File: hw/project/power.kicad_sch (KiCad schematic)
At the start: 28 parts, among them Q1 MOSFET, N-CH, SINGLE, 120A, 6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, Q2 MOSFET, N-CH, SINGLE, 120A, 6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, U1 TLV74033PDBVR, U3 LM74502DDFR, U4 LMR51610XDBVR

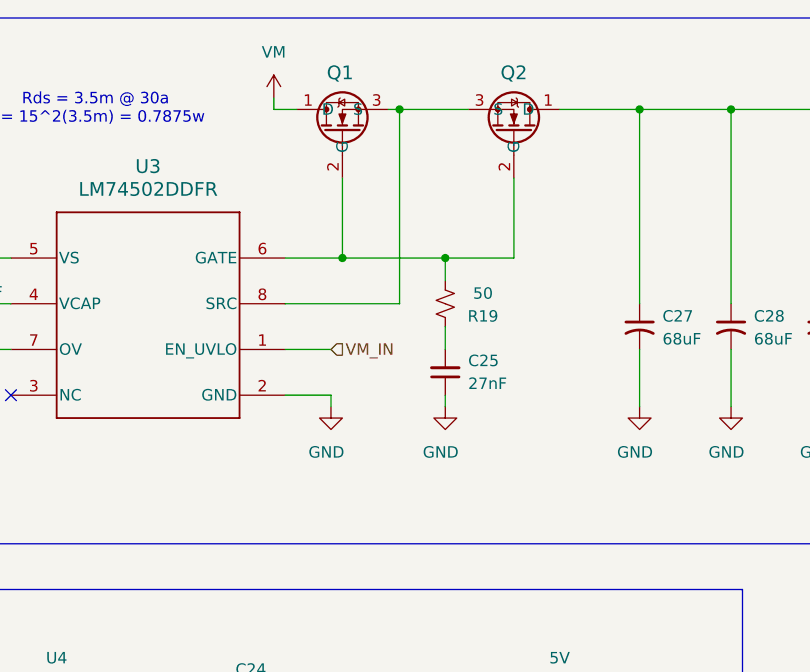
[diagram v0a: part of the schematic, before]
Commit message: Wire PWR BTN
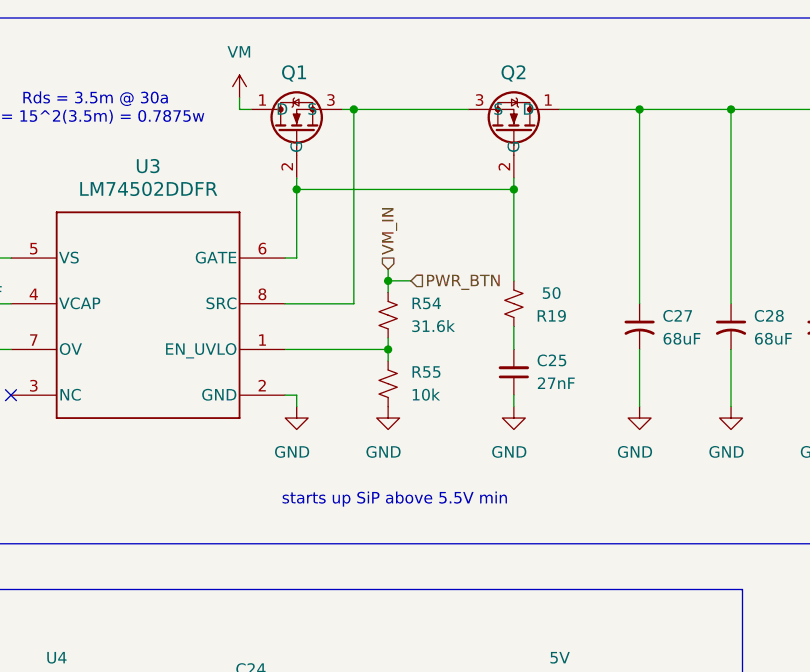
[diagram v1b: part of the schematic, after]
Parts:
- added R54: 31.6k, symbol Device:R_Small_US
- added R55: 10k, symbol Device:R_Small_US
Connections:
- net GND: now also R55.2
- net VM_IN renamed PWR_BTN
- net PWR_BTN: now also R54.1; no longer U3.1 (EN_UVLO)
- new net: R54.2, R55.1, U3.1 (EN_UVLO)
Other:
- note added: "starts up SiP above 5.5V min"
- moved on the sheet: C25, Q1, R19

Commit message: Add comment to 5V buck
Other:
- note added: "Rds = 3.5m @ 30a P = 30^2(3.5m) = 3.15w"
- note added: "are you sure this gives 5V? can you document the calculation for getting 5V output?"
- note removed: "Rds = 3.5m @ 30a P = 15^2(3.5m) = 0.7875w"
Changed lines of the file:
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@@
 		)
 	)
-	(text "Rds = 3.5m @ 30a\nP = 15^2(3.5m) = 0.7875w"
+	(text "Rds = 3.5m @ 30a\nP = 30^2(3.5m) = 3.15w"
 		(exclude_from_sim no)
 		(at 89.408 33.02 0)
@@
 			)
 		)
+	)
+	(text "are you sure this gives 5V?\n\ncan you document the calculation\nfor getting 5V output?"
+		(exclude_from_sim no)
+		(at 127 129.032 0)
+		(effects
+			(font
+				(size 1.27 1.27)
+				(color 255 4 4 1)
+			)
+		)

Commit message: Leo's final revisions to (mostly) periphs
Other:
- note added: "<- add (hookable, if appropriate) test points where you can in the Power sheet"
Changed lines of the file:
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@@
+		)
+	)
+	(text "<- add (hookable, if appropriate) test points \nwhere you can in the Power sheet"
+		(exclude_from_sim no)
+		(at 241.808 108.458 0)
+		(effects
+			(font
+				(size 1.27 1.27)
+				(color 255 4 4 1)
+			)
 		)
 	)

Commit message: Update sheet settings
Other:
- company: (none) -> Electrium Mobility
- title: (none) -> ESC 2026 - Power
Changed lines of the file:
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@@
 	(paper "A4")
 	(title_block
+		(title "ESC 2026 - Power")
 		(date "2026-02-20")
-		(rev "1")
+		(rev "v3")
+		(company "Electrium Mobility")
 		(comment 1 "Author: Nelson Mei, Arnav Shah, Eleanor Wang")
 	)

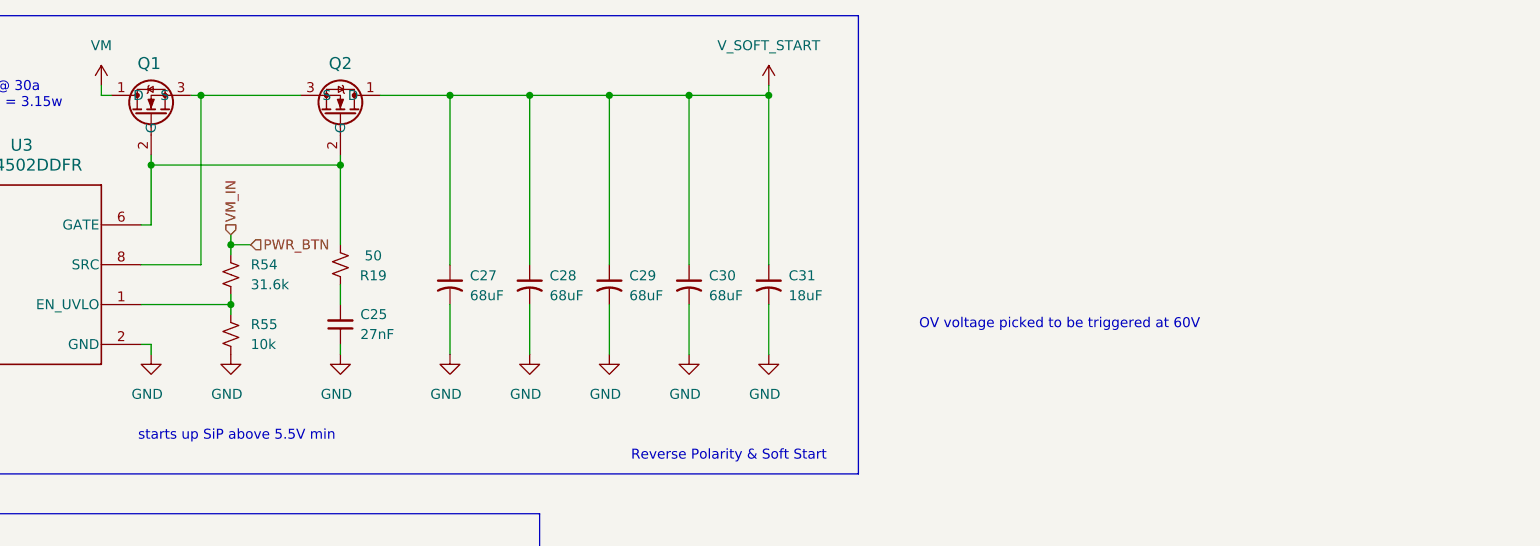
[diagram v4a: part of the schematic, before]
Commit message: Rework power button to power slide switch, no footprint/part yetgit add .
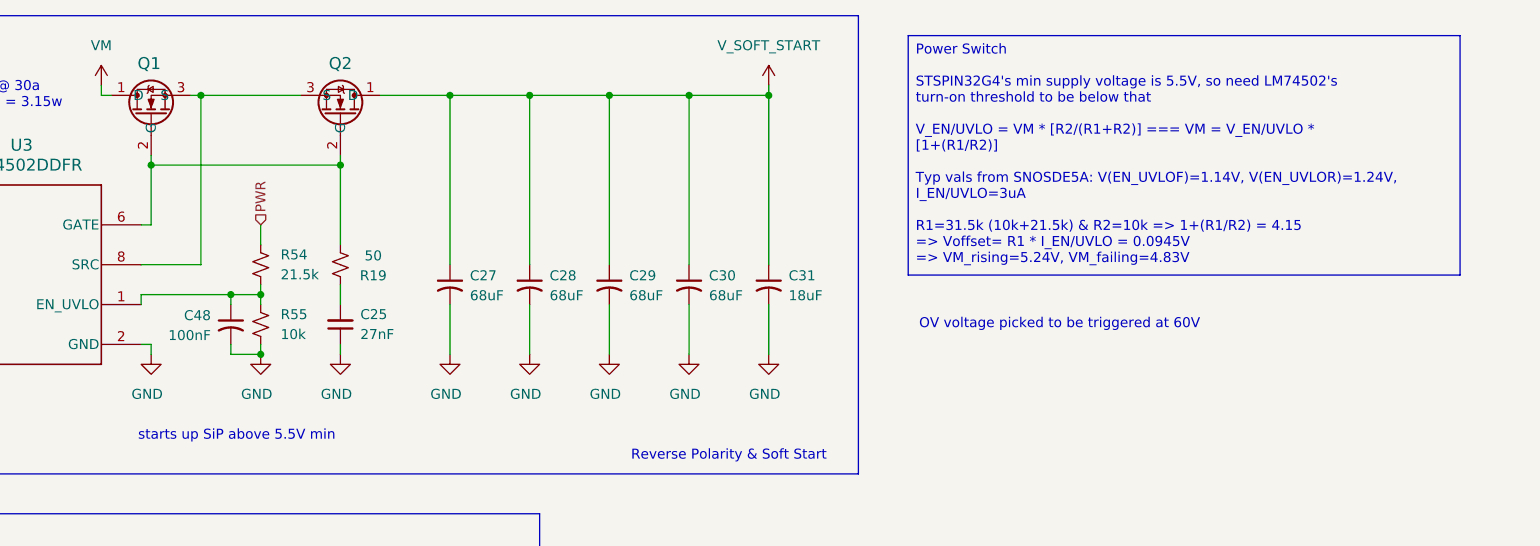
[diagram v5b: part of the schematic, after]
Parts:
- added C48: 100nF, symbol Device:C_Small_US
- R54: value 31.6k -> 21.5k
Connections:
- net GND: now also C48.2
- net at R54.2, R55.1, U3.1 (EN_UVLO): now also C48.1
- net PWR_BTN renamed VM_IN
- net VM_IN: no longer R54.1
- new net PWR: R54.1
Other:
- moved on the sheet: R54, R55
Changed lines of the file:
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@@
 		)
 	)
-	(text "starts up SiP above 5.5V min"
+	(text "starts up SiP above 5.5V min\n"
 		(exclude_from_sim no)
 		(at 122.682 76.454 0)
@@
 		)
 	)
+	(text_box "Power Switch\n\nSTSPIN32G4's min supply voltage is 5.5V, so need LM74502's turn-on threshold to be below that\n\nV_EN/UVLO = VM * [R2/(R1+R2)] === VM = V_EN/UVLO * [1+(R1/R2)]\n\nTyp vals from SNOSDE5A: V(EN_UVLOF)=1.14V, V(EN_UVLOR)=1.24V, I_EN/UVLO=3uA\n\nR1=31.5k (10k+21.5k) & R2=10k => 1+(R1/R2) = 4.15\n=> Voffset= R1 * I_EN/UVLO = 0.0945V\n=> VM_rising=5.24V, VM_failing=4.83V"
+		(exclude_from_sim no)
+		(at 208.28 25.4 0)
+		(size 70.358 30.5285)
+		(margins 0.9525 0.9525 0.9525 0.9525)
+		(stroke
+			(width 0)
+			(type solid)
+		)
+		(fill
+			(type none)
+		)
+		(effects
+			(font
+				(size 1.27 1.27)
+			)
+			(justify left top)
+		)
+	)
 	(junction
 		(at 135.89 41.91)
@@
 	)
 	(junction
-		(at 123.19 116.84)
+		(at 121.92 58.42)
 		(diameter 0)
 		(color 0 0 0 0)
 	)
 	(junction
-		(at 121.92 52.07)
+		(at 123.19 116.84)
 		(diameter 0)
 		(color 0 0 0 0)
@@
 	)
 	(junction
-		(at 121.92 59.69)
+		(at 60.96 49.53)
 		(diameter 0)
 		(color 0 0 0 0)
 	)
 	(junction
-		(at 60.96 49.53)
+		(at 105.41 160.02)
 		(diameter 0)
 		(color 0 0 0 0)
 	)
 	(junction
-		(at 105.41 160.02)
+		(at 125.73 66.04)
 		(diameter 0)
 		(color 0 0 0 0)
@@
 	)
 	(junction
+		(at 125.73 58.42)
+		(diameter 0)
+		(color 0 0 0 0)
+	)
+	(junction
 		(at 71.12 49.53)
 		(diameter 0)
@@
 	(wire
 		(pts
+			(xy 121.92 58.42) (xy 121.92 59.69)
+		)
+		(stroke
+			(width 0)
+			(type default)
+		)
+	)
+	(wire
+		(pts
 			(xy 118.11 33.02) (xy 130.81 33.02)
 		)
@@
 	(wire
 		(pts
-			(xy 121.92 59.69) (xy 121.92 60.96)
-		)
-		(stroke
-			(width 0)
-			(type default)
-		)
-	)
-	(wire
-		(pts
 			(xy 67.31 160.02) (xy 69.85 160.02)
 		)
@@
 	(wire
 		(pts
-			(xy 121.92 58.42) (xy 121.92 59.69)
+			(xy 125.73 57.15) (xy 125.73 58.42)
 		)
 		(stroke
@@
 	(wire
 		(pts
-			(xy 110.49 59.69) (xy 121.92 59.69)
+			(xy 110.49 58.42) (xy 121.92 58.42)
 		)
 		(stroke
@@
 	(wire
 		(pts
-			(xy 121.92 52.07) (xy 121.92 53.34)
+			(xy 125.73 49.53) (xy 125.73 52.07)
 		)
 		(stroke
@@
 	(wire
 		(pts
-			(xy 121.92 52.07) (xy 124.46 52.07)
+			(xy 57.15 106.68) (xy 67.31 106.68)
 		)
 		(stroke
@@
 		)
 	)
-	(wire
+	(polyline
 		(pts
-			(xy 57.15 106.68) (xy 67.31 106.68)
+			(xy 21.59 86.36) (xy 21.59 137.16)
 		)
 		(stroke
@@
 		)
 	)
-	(polyline
+	(wire
 		(pts
-			(xy 21.59 86.36) (xy 21.59 137.16)
+			(xy 121.92 66.04) (xy 125.73 66.04)
 		)
 		(stroke
@@
 	(wire
 		(pts
+			(xy 125.73 58.42) (xy 125.73 59.69)
+		)
+		(stroke
+			(width 0)
+			(type default)
+		)
+	)
+	(wire
+		(pts
 			(xy 105.41 33.02) (xy 106.68 33.02)
 		)
@@
 	(wire
 		(pts
+			(xy 110.49 58.42) (xy 110.49 59.69)
+		)
+		(stroke
+			(width 0)
+			(type default)
+		)
+	)
+	(wire
+		(pts
 			(xy 105.41 167.64) (xy 105.41 170.18)
 		)
@@
 	(wire
 		(pts
+			(xy 121.92 58.42) (xy 125.73 58.42)
+		)
+		(stroke
+			(width 0)
+			(type default)
+		)
+	)
+	(wire
+		(pts
 			(xy 67.31 106.68) (xy 69.85 106.68)
 		)
@@
 	(wire
 		(pts
-			(xy 121.92 50.8) (xy 121.92 52.07)
+			(xy 123.19 101.6) (xy 123.19 105.41)
 		)
 		(stroke
@@
 		)
 	)
-	(wire
+	(polyline
 		(pts
-			(xy 123.19 101.6) (xy 123.19 105.41)
+			(xy 161.29 86.36) (xy 161.29 137.16)
 		)
 		(stroke
@@
 		)
 	)
-	(polyline
+	(wire
 		(pts
-			(xy 161.29 86.36) (xy 161.29 137.16)
+			(xy 125.73 64.77) (xy 125.73 66.04)
 		)
 		(stroke
@@
 	(wire
 		(pts
-			(xy 105.41 158.75) (xy 105.41 160.02)
+			(xy 121.92 64.77) (xy 121.92 66.04)
 		)
 		(stroke
@@
 		)
 	)
-	(hierarchical_label "VM_IN"
-		(shape input)
-		(at 31.75 46.99 90)
-		(effects
-			(font
-				(size 1.27 1.27)
-			)
-			(justify left)
+	(wire
+		(pts
+			(xy 105.41 158.75) (xy 105.41 160.02)
+		)
+		(stroke
+			(width 0)
+			(type default)
 		)
 	)
 	(hierarchical_label "VM_IN"
 		(shape input)
-		(at 121.92 50.8 90)
+		(at 31.75 46.99 90)
 		(effects
 			(font
@@
 		)
 	)
-	(hierarchical_label "PWR_BTN"
+	(hierarchical_label "PWR"
 		(shape input)
-		(at 124.46 52.07 0)
+		(at 125.73 49.53 90)
 		(effects
 			(font
@@
 	(symbol
 		(lib_id "power:GND")
-		(at 121.92 66.04 0)
+		(at 125.73 66.04 0)
 		(unit 1)
 		(body_style 1)
@@
 		(dnp no)
 		(property "Reference" "#PWR078"
-			(at 121.92 72.39 0)
+			(at 125.73 72.39 0)
 			(hide yes)
 			(show_name no)
@@
 		)
 		(property "Value" "GND"
-			(at 121.412 71.12 0)
+			(at 125.222 71.12 0)
 			(show_name no)
 			(do_not_autoplace no)
@@
 		)
 		(property "Footprint" ""
-			(at 121.92 66.04 0)
+			(at 125.73 66.04 0)
 			(hide yes)
 			(show_name no)
@@
 		)
 		(property "Datasheet" ""
-			(at 121.92 66.04 0)
+			(at 125.73 66.04 0)
 			(hide yes)
 			(show_name no)
@@
 		)
 		(property "Description" "Power symbol creates a global label with name \"GND\" , ground"
-			(at 121.92 66.04 0)
+			(at 125.73 66.04 0)
 			(hide yes)
 			(show_name no)
@@
 	(symbol
 		(lib_id "Device:R_Small_US")
-		(at 121.92 63.5 0)
+		(at 125.73 62.23 0)
 		(unit 1)
 		(body_style 1)
@@
 		(fields_autoplaced yes)
 		(property "Reference" "R55"
-			(at 124.46 62.2299 0)
+			(at 128.27 60.9599 0)
 			(show_name no)
 			(do_not_autoplace no)
@@
 		)
 		(property "Value" "10k"
-			(at 124.46 64.7699 0)
+			(at 128.27 63.4999 0)
 			(show_name no)
 			(do_not_autoplace no)
@@
 		)
 		(property "Footprint" ""
-			(at 121.92 63.5 0)
+			(at 125.73 62.23 0)
 			(hide yes)
 			(show_name no)
@@
 		)
 		(property "Datasheet" ""
-			(at 121.92 63.5 0)
+			(at 125.73 62.23 0)
 			(hide yes)
 			(show_name no)
@@
 		)
 		(property "Description" ""
-			(at 121.92 63.5 0)
+			(at 125.73 62.23 0)
 			(hide yes)
 			(show_name no)
@@
 	)
 	(symbol
+		(lib_id "Device:C_Small_US")
+		(at 121.92 62.23 0)
+		(mirror y)
+		(unit 1)
+		(body_style 1)
+		(exclude_from_sim no)
+		(in_bom yes)
+		(on_board yes)
+		(in_pos_files yes)
+		(dnp no)
+		(property "Reference" "C48"
+			(at 119.38 61.0869 0)
+			(show_name no)
+			(do_not_autoplace no)
+			(effects
+				(font
+					(size 1.27 1.27)
+				)
+				(justify left)
+			)
+		)
+		(property "Value" "100nF"
+			(at 119.38 63.6269 0)
+			(show_name no)
+			(do_not_autoplace no)
+			(effects
+				(font
+					(size 1.27 1.27)
+				)
+				(justify left)
+			)
+		)
+		(property "Footprint" ""
+			(at 121.92 62.23 0)
+			(hide yes)
+			(show_name no)
+			(do_not_autoplace no)
+			(effects
+				(font
+					(size 1.27 1.27)
+				)
+			)
+		)
+		(property "Datasheet" ""
+			(at 121.92 62.23 0)
+			(hide yes)
+			(show_name no)
+			(do_not_autoplace no)
+			(effects
+				(font
+					(size 1.27 1.27)
+				)
+			)
+		)
+		(property "Description" "capacitor, small US symbol"
+			(at 121.92 62.23 0)
+			(hide yes)
+			(show_name no)
+			(do_not_autoplace no)
+			(effects
+				(font
+					(size 1.27 1.27)
+				)
+			)
+		)
+		(pin "2"
+		)
+		(pin "1"
+		)
+		(instances
+			(project "esc"
+				(path "/86a17c4d-db96-42a1-af84-d43fe593f4e6/5338eeb3-4021-4459-b70f-dab93d7c7a1a"
+					(reference "C48")
+					(unit 1)
+				)
+			)
+		)
+	)
+	(symbol
 		(lib_id "power:GND")
 		(at 160.02 66.04 0)
@@
 	(symbol
 		(lib_id "Device:R_Small_US")
-		(at 121.92 55.88 0)
+		(at 125.73 54.61 0)
 		(unit 1)
 		(body_style 1)
@@
 		(fields_autoplaced yes)
 		(property "Reference" "R54"
-			(at 124.46 54.6099 0)
+			(at 128.27 53.3399 0)
 			(show_name no)
 			(do_not_autoplace no)
@@
 			)
 		)
-		(property "Value" "31.6k"
-			(at 124.46 57.1499 0)
+		(property "Value" "21.5k"
+			(at 128.27 55.8799 0)
 			(show_name no)
 			(do_not_autoplace no)
@@
 		)
 		(property "Footprint" ""
-			(at 121.92 55.88 0)
+			(at 125.73 54.61 0)
 			(hide yes)
 			(show_name no)
@@
 		)
 		(property "Datasheet" ""
-			(at 121.92 55.88 0)
+			(at 125.73 54.61 0)
 			(hide yes)
 			(show_name no)
@@
 		)
 		(property "Description" ""
-			(at 121.92 55.88 0)
+			(at 125.73 54.61 0)
 			(hide yes)
 			(show_name no)

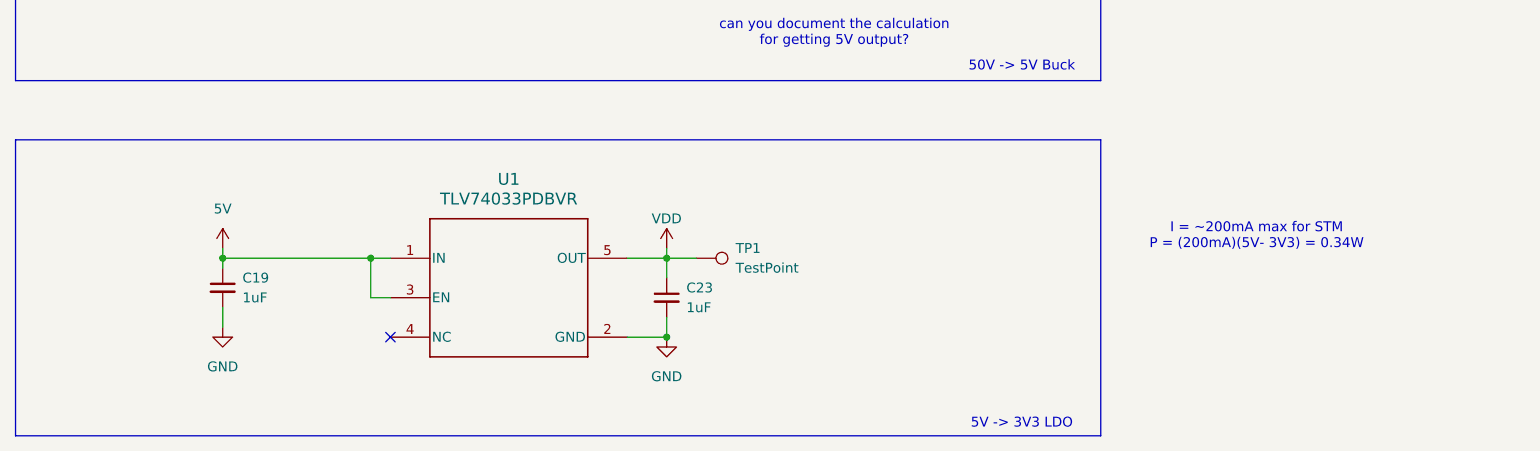
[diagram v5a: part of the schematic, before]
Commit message: Deleting 5V to 3V3 LDO. Replace all references to net '3V3' with 'VDD.'
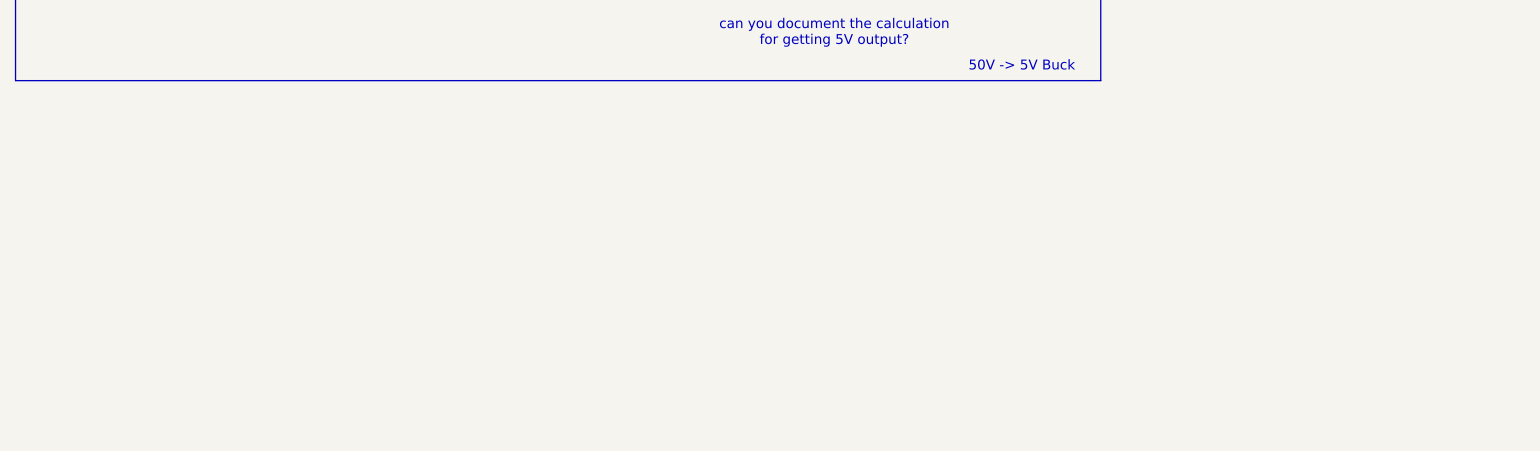
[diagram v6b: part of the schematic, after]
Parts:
- removed C19, C23: 1uF, Capacitor_SMD:C_0603_1608Metric, symbol Device:C_Small
- removed TP1: TestPoint, TestPoint:TestPoint_Pad_D1.0mm, symbol Connector:TestPoint
- removed U1: TLV74033PDBVR, TLV74033PDBVR:DBV0005A-MFG, symbol TLV74033PDBVR:TLV74033PDBVR
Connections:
- no-connect marks 2 -> 1
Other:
- note removed: "5V -> 3V3 LDO"
- note removed: "I = ~200mA max for STM P = (200mA)(5V- 3V3) = 0.34W"

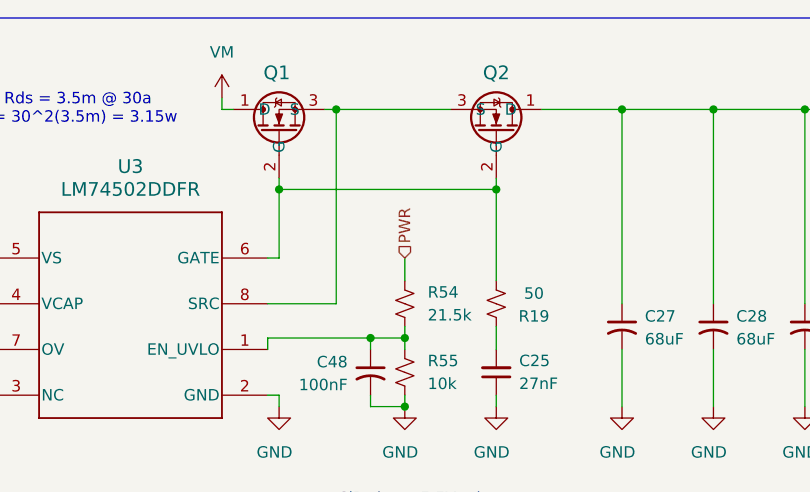
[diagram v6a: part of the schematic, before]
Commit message: Prettify root sheet
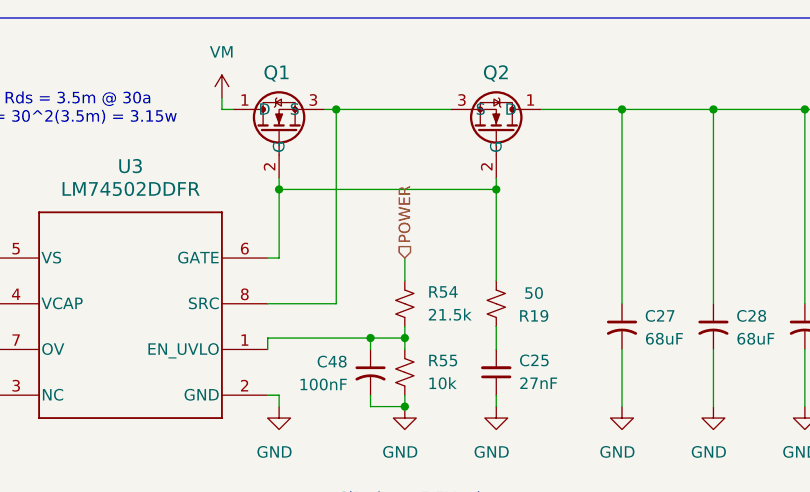
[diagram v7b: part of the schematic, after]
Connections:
- net PWR renamed POWER
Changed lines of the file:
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@@
 		)
 	)
-	(hierarchical_label "PWR"
+	(hierarchical_label "POWER"
 		(shape input)
 		(at 125.73 49.53 90)
